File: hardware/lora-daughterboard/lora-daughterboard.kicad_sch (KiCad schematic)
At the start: 65 parts, among them J2 USB4110GFA, J6 Conn_01x04, J8 CON-SMA-EDGE-S, U14 E220-900MM22S, U22 W25Q64JVXGIQ TR, U28 ESP32-S3, U3 TPS62913RPUR, Y5 ECS-.327-6-16R-TR, Y6 ECS-400-10-37B2-CKY-TR

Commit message: hardware: BOM-cost pass across all four boards
Component changes from a cross-board cost review. Per-board component cost
(USD @~100qty): rocket $86.21 -> $61.39, base station $35.91 -> $29.89, with
the LoRa daughterboard and GNSS SAM-M10Q board added to the shared BOM.

Memory architecture
  - Rocket: MR25H10 MRAM deleted; the log ring moves to in-package PSRAM.
    ESP32-S3 -> ESP32-S3RH2 (2 MB quad PSRAM, no in-package flash, same land
    pattern; SPICS1/GPIO26 was already unconnected on every board).
    Persistence across boots is knowingly given up.
  - Rocket NAND F35SQB004G-WWT -> GD5F2GQ5UEYIGR: pin- and footprint-identical
    (verified against the U11 land pattern), 4 Gbit -> 2 Gbit, $11.61 -> $3.50.
    Needs the 4096 -> 2048 B page migration in firmware.
  - Base station: dedicated log flash deleted entirely. It wrote one ~183 B CSV
    row per received packet at the 2 Hz downlink (~366 B/s, and only while a
    flight is active), so 256 MB was ~204 hours of headroom. The firmware
    already falls back to the existing SPIFFS partition, so this promotes a
    tested path rather than needing new code.
  - Boot flash W25Q64JVXGIQ -> W25Q128JVSIQ on all four positions: 16 MB for
    LESS money ($3.10 -> $2.21). SCHEMATIC ONLY - the boards still need
    "Update PCB from Schematic" plus re-placement, since SOIC-8 208mil is 2.2x
    the DFN's area. The DFN's 9th (exposed) pad was a redundant GND tie; pin 4
    is GND on all four, so nothing is lost.

Power
  - LoRa + GNSS keep TPS62913 (low-noise, RF rails). The rocket briefly moved
    to it and was REVERTED to TPS62152: the TPS62913 is forced-PWM with 5 mA
    quiescent, which would have raised the pad-idle floor ~6x against the
    light-sleep work.
  - Base load switch TPS22810 -> TPS22918 (identical footprint and pin order;
    pin 3 EN/UVLO -> ON is safe because it was driven as a plain enable).
    CT cap 10 nF -> 2.2 nF to match the rocket's ramp; R8 (QOD->VOUT) deleted.
  - LoRa gains a 7.5k S-CONF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
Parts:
- removed CR1, CR3: PMEG2010ER_115, Footprints:DIODE_PMEG2010ER_115_NEX, symbol Custom:PMEG2010ER_115
- removed L1: ASPI-0530HI-2R2M-T2, Footprints:IND_ASPI-0530HI-2R2M-T2, symbol Custom:ASPI-0530HI-2R2M-T2
- added CR1, CR3: CUS10S30_H3F, USC_TOS, symbol Custom:CUS10S30_H3F
- added L8: VLS3012CX-2R2M-1, Footprints:IND_VLS3012CX-2R2M-1, symbol Custom:VLS3012CX-2R2M-1
- added R8: 7.5 k, Resistor_SMD:R_0402_1005Metric, symbol Device:R_US
- C102: value 47 uF -> 10 uF
- C106: value 22 uF -> 10 uF
- C16: value 10 uF -> 22 uF
- U22: value W25Q64JVXGIQ TR -> W25Q128JVSIQ; footprint Footprints:DFN_XGIQ TR_WIN -> Footprints:SOIC-8_W25Q128JVSIQ
- U28: value ESP32-S3 -> ESP32-S3RH2
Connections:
- net +BATT: now also CR3.2
- net GND: now also R8.2; no longer U3.10 (S-CONF)
- net VBUS: now also CR1.2
- net VSYS: now also CR1.1, CR3.1
- net at C11.1, C13.1, FB1.1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: now also L8.2
- net at U3.2 (SW): now also L8.1
- new net: R8.1, U3.10 (S-CONF)
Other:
- moved on the sheet: R4

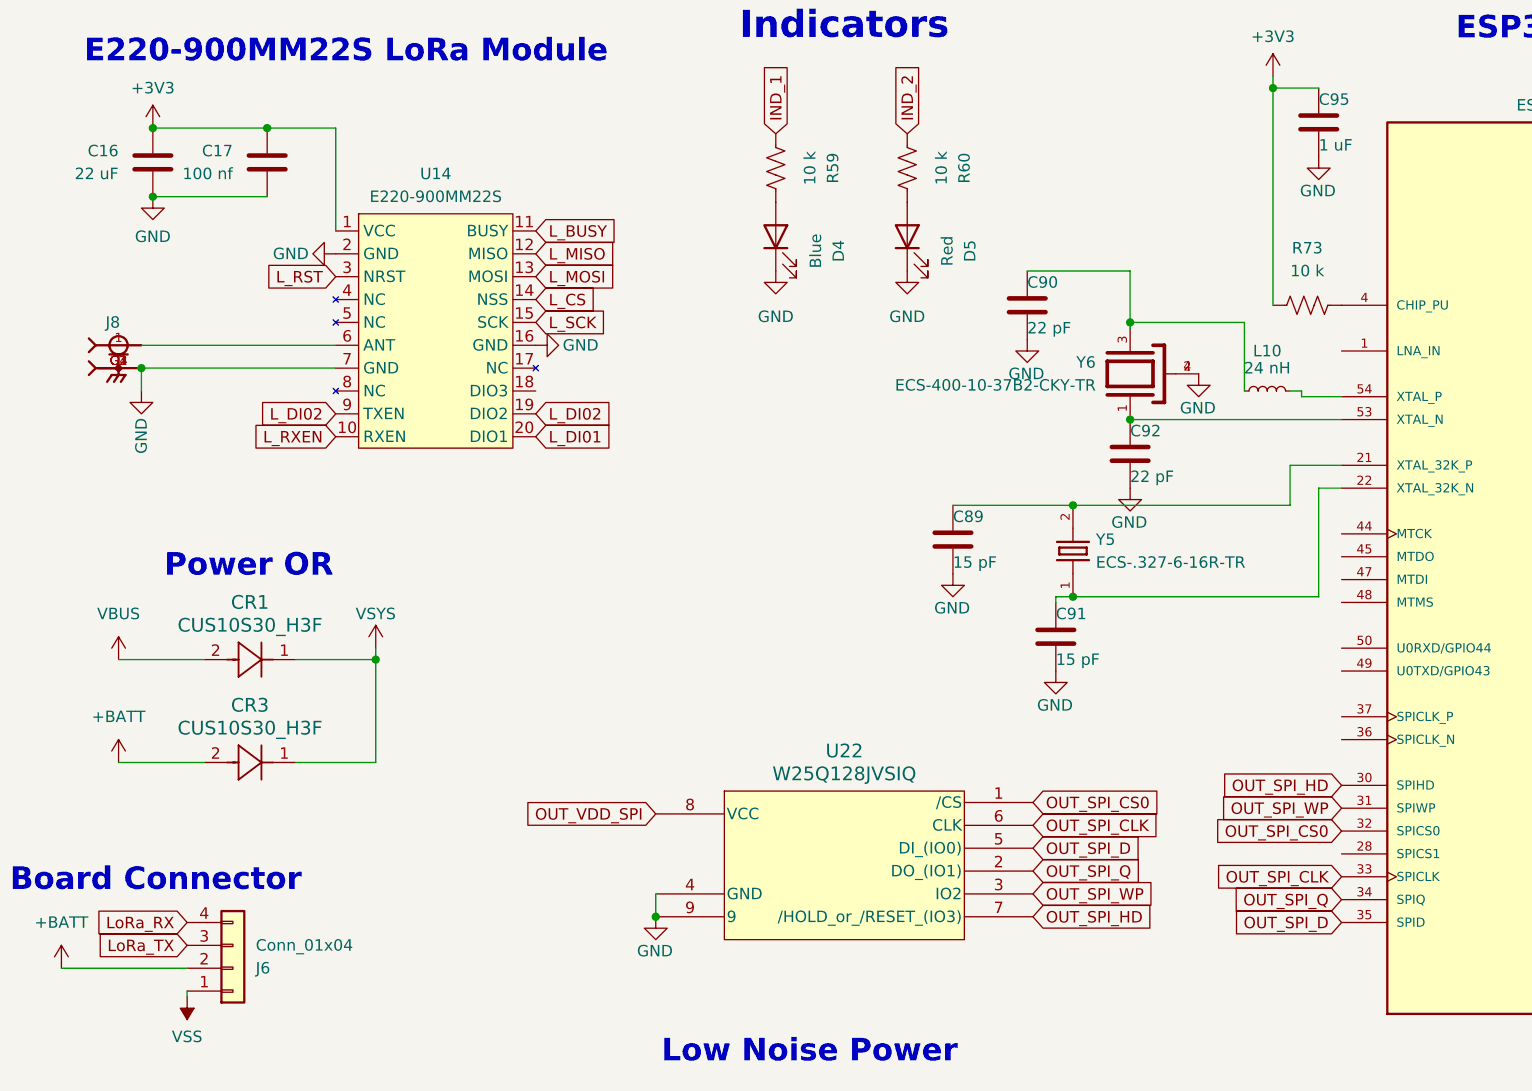
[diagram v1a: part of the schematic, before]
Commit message: hardware: battery protection, boost swap, and a capacitor voltage audit
Base station power chain, all verified against exported netlists:

- Protection: MAX17303G+ gauge/protector and its NTMD6N02R2G FET pair
  replaced by DW01A + 2x FS8205A. The MAX17303 had no firmware driver and
  the board never had a working coulomb counter, so state of charge already
  came from the voltage curve in bs_battery_soc.h; it now reads a 1M/1M
  divider on GPIO1. The FETs move from the positive rail to the negative
  one because the DW01A has no charge pump, so board ground is now P-,
  separated from the cell's B- by the FET stack. Two FS8205A in parallel
  put the 150 mV overcurrent trip at ~4.8-6.0 A instead of ~2.4-3.0 A.
  TH1 moves onto the BQ21040's TS pin, replacing a fixed 10k that had been
  defeating thermal charge cutoff.

- V_LORA retargeted 7.49 V -> 4.95 V and LM5157QRTERQ1 -> TPS61023DRLR.
  Nothing needed 7.4 V (everything downstream is 3.3 V behind the
  TPS62913), while an RFD868x-class radio is 5 V nominal with a 6 V
  absolute maximum, so the old rail put it permanently out of reach. Being
  synchronous and internally compensated also dropped D2, C35-C38 and R10.
  Inductor stays the fleet 2.2 uH: inside TI's 0.37-2.9 uH range and the
  only value meeting their ripple-under-40%-of-average guidance at load.

- Keystone 1043P holder -> MYOUNG BH-18650-A5BJ001-2D. Terminal pitch
  72.30 vs 72.22 mm, so the battery nets did not move; BT2 is rotated 180
  degrees because this part's positive end is mirrored.

Across all four boards:

- Every crystal was mis-loaded. 32.768 kHz parts saw ~9 pF against a 6 pF
  spec and the 40 MHz saw 12.5 pF against 10 pF, both pulling slow. Moved
  to Seiko SC-32S (12.5 pF) with 22 pF load caps, and the 40 MHz caps to
  18 pF. The tolerance being paid for had been swamped several times over.

- Capacitor voltage audit, new Min V rating column in the BOM. Three parts
  were operating outside their rating on 8.4 V rails: 47 uF and 100 u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
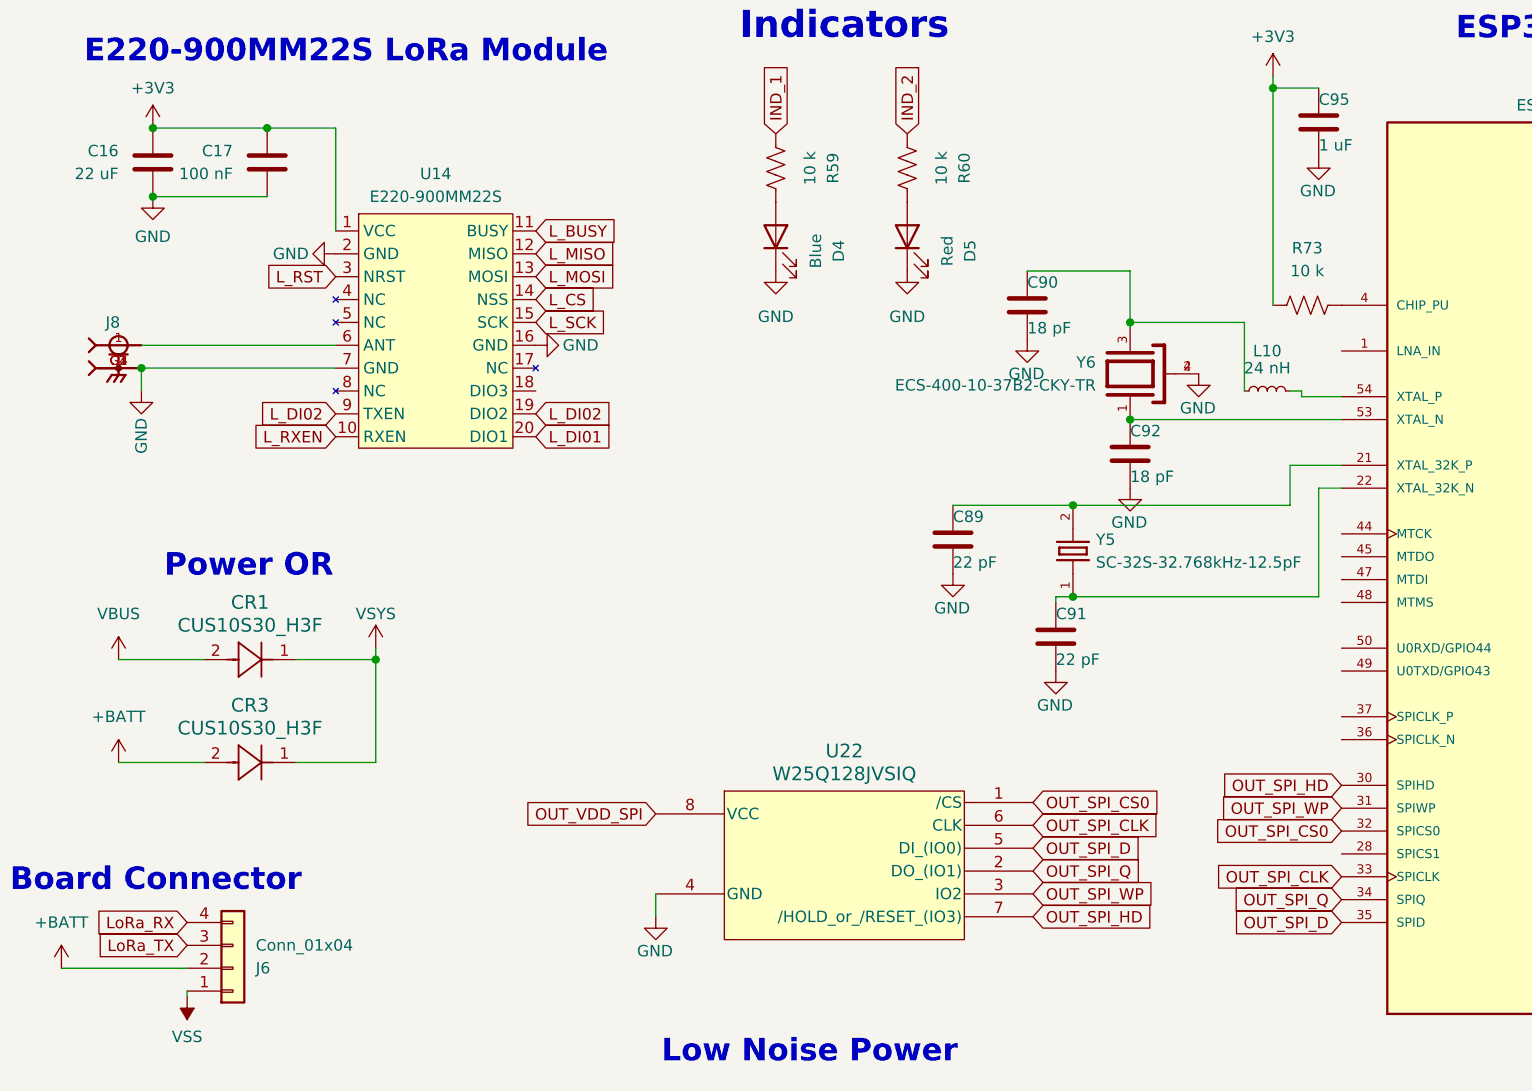
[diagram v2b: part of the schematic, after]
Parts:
- C17: value 100 nf -> 100 nF
- C89, C91: value 15 pF -> 22 pF
- C90, C92: value 22 pF -> 18 pF
- CR1, CR3: footprint USC_TOS -> Footprints:USC_TOS
- U22: symbol Custom:W25Q64JVXGIQ_TR -> Custom:W25Q128JVSIQ
- Y5: value ECS-.327-6-16R-TR -> SC-32S-32.768kHz-12.5pF; footprint Footprints:XTAL_ECS-.327-6-16R-TR -> Footprints:XTAL_SC-32S_3215; symbol Custom:ECS-.327-6-16R-TR -> Custom:SC-32S-32.768kHz-12.5pF
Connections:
- net GND: no longer U22.9
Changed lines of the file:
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@@
 	)
 	(junction
-		(at 86.36 118.745)
-		(diameter 0)
-		(color 0 0 0 0)
-	)
-	(junction
 		(at 70.485 160.655)
 		(diameter 0)
@@
 			)
 		)
-		(property "Value" "22 pF"
+		(property "Value" "18 pF"
 			(at 127.635 53.34 0)
 			(show_name no)
@@
 			)
 		)
-		(property "Footprint" "USC_TOS"
+		(property "Footprint" "Footprints:USC_TOS"
 			(at 36.195 90.17 0)
 			(hide yes)
@@
 			)
 		)
-		(property "Footprint" "USC_TOS"
+		(property "Footprint" "Footprints:USC_TOS"
 			(at 36.195 101.6 0)
 			(hide yes)
@@
 			)
 		)
-		(property "Value" "15 pF"
+		(property "Value" "22 pF"
 			(at 130.81 90.17 0)
 			(show_name no)
@@
 	)
 	(symbol
-		(lib_id "Custom:W25Q64JVXGIQ_TR")
+		(lib_id "Custom:W25Q128JVSIQ")
 		(at 63.5 112.395 0)
 		(unit 1)
@@
 			)
 		)
-		(pin "9"
-		)
 		(pin "8"
 		)
@@
 			)
 		)
-		(property "Value" "22 pF"
+		(property "Value" "18 pF"
 			(at 139.065 69.85 0)
 			(show_name no)
@@
 			)
 		)
-		(property "Value" "15 pF"
+		(property "Value" "22 pF"
 			(at 119.38 79.375 0)
 			(show_name no)
@@
 	)
 	(symbol
-		(lib_id "Custom:ECS-.327-6-16R-TR")
+		(lib_id "Custom:SC-32S-32.768kHz-12.5pF")
 		(at 132.715 78.105 90)
 		(unit 1)
@@
 			)
 		)
-		(property "Value" "ECS-.327-6-16R-TR"
+		(property "Value" "SC-32S-32.768kHz-12.5pF"
 			(at 135.255 79.3749 90)
 			(show_name no)
@@
 			)
 		)
-		(property "Footprint" "Footprints:XTAL_ECS-.327-6-16R-TR"
+		(property "Footprint" "Footprints:XTAL_SC-32S_3215"
 			(at 132.715 78.105 0)
 			(hide yes)
@@
 			)
 		)
-		(property "Value" "100 nf"
+		(property "Value" "100 nF"
 			(at 39.37 36.1949 0)
 			(show_name no)

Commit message: hardware(lora): capacitor MPNs in KiCad + COUT 2x47uF -> 3x22uF
Capacitors: all 27 now carry MPN / Mfr / MinVRating fields, sourced from
Circuit Board BOMs/TinkerRocket_CrossBoard_BOM.xlsx (sheet "Cross-Board
BOM"). Field names mirror the spreadsheet columns so the two stay
diff-checkable; MinVRating is the design requirement, not the part's own
rating (the 470 nF requirement is 6.3 V while CL05A474KP5NNNC is a 10 V
part).

COUT: C11/C13 were CL21A476MQYNNNE (47 uF, 6.3 V X5R, 0805) on
Net-(U3-VO). At 3.3 V that is 52% of rated voltage, where the class
derates 55-70% -- roughly 28-42 uF against the TPS62913's 40 uF minimum
effective COUT. Revalued to CL21A226MOQNNNE (22 uF, 16 V), already a
stocked line on this board, and a third added (C14 + #PWR096 + junction
on the VO wire) for ~42-53 uF. Matches TI Table 8-5 (3 x 22 uF 0805).

Verified with kicad-cli under identical project context: nets unchanged
apart from the intended C14 addition (Net-(U3-VO) = C11.1 C13.1 C14.1
FB1.1 L8.2 R4.2 U3.3), ERC 301 -> 304 with the error count unchanged at
32 -- the three new warnings are endpoint_off_grid / lib_symbol_mismatch
inherited from the C13 and #PWR013 templates they were cloned from.

PCB not touched: needs Update PCB from Schematic, then place C14 (free
F.Cu slot at (93.40,128.8), inside the existing Net-(U3-VO) pour) and
re-route C95, whose schematic side moved to the CHIP_PU node.

Co-Authored-By: Claude Opus 5 <noreply@anthropic.com>
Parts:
- added C14: 22 uF, Capacitor_SMD:C_0805_2012Metric, symbol Device:C
- C10: MPN (none) -> CL05A474KP5NNNC; Mfr (none) -> Samsung; MinVRating (none) -> 6.3 V
- C100, C105, C95, C96: MPN (none) -> CL05A105KO5NNNC; Mfr (none) -> Samsung; MinVRating (none) -> 16 V
- C101, C103, C104, C17, C99: MPN (none) -> CL05B104KO5NNNC; Mfr (none) -> Samsung; MinVRating (none) -> 16 V
- C102, C106, C97: MPN (none) -> CL05A106MQ5NUNC; Mfr (none) -> Samsung; MinVRating (none) -> 6.3 V
- C11, C13: value 47 uF -> 22 uF; MPN (none) -> CL21A226MOQNNNE; Mfr (none) -> Samsung; MinVRating (none) -> 16 V
- C12, C15, C16, C8, C9: MPN (none) -> CL21A226MOQNNNE; Mfr (none) -> Samsung; MinVRating (none) -> 16 V
- C7: MPN (none) -> CC0402KRX7R9BB222; Mfr (none) -> Yageo; MinVRating (none) -> 16 V
- C89, C91: MPN (none) -> CL05C220JB5NNNC; Mfr (none) -> Samsung; MinVRating (none) -> 6.3 V
- C90, C92: MPN (none) -> CL05C180JB5NNNC; Mfr (none) -> Samsung; MinVRating (none) -> 6.3 V
- C98: MPN (none) -> CL05B103KB5NNNC; Mfr (none) -> Samsung; MinVRating (none) -> 6.3 V
- FB1: value WE-CBA_0805 -> 782853200
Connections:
- net +3V3: now also R73.1; no longer C95.1, R73.2
- net GND: now also C14.2
- net at U28.4 (CHIP_PU): now also C95.1, R73.2; no longer R73.1
- net at C11.1, C13.1, FB1.1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: now also C14.1
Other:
- moved on the sheet: C95, R73

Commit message: hardware(lora): VDD_SPI -- flash to +3V3, decoupling to the pin
Pre-fab review finding 4. In 3.3 V mode VDD_SPI is not a regulator: the
S3 datasheet Table 5-3 describes it as "VDD_SPI powered by VDD3P3_RTC via
R_SPI", 14 ohm typ, and footnote 2 bounds the load with

    VDD3P3_RTC > VDD_flash_min + I_flash_max * R_SPI

On the S3RH2 the in-package 2 MB quad PSRAM already sits on that node
(Table 1-1), so I_flash_max is flash plus PSRAM. Flash alone passes
comfortably (2.7 + 0.025*14 = 3.05 V required, 3.3 V available); flash
plus PSRAM at ~30 mA does not (3.47 V required). Espressif publishes no
in-package PSRAM current figure, so that second number is an estimate --
this change is defensive, removing a coupling where enabling
CONFIG_SPIRAM later would silently starve the boot flash.

  - U22 pin 8 (VCC): OUT_VDD_SPI -> +3V3
  - C18 100 nF added on +3V3 as the flash's local decoupling
  - OUT_VDD_SPI left as {U28.29, C96 1 uF, C97 10 uF}, serving only PSRAM

C97 stays at 10 uF deliberately. The HDG's "do not add excessively large
capacitors" is driven by startup delay through the 14 ohm and by
light-sleep wake recovery; neither applies here (VDD_SPI settles in
~400 us against a 2-3 ms CHIP_PU release, and this board never
light-sleeps). Meanwhile the 14 ohm makes VDD_SPI the highest-source-
impedance rail on the board, where local bulk is worth most.

Verified: OUT_VDD_SPI = {C96.1, C97.1, U28.29}; ERC error count unchanged
at 32 (one power_pin_not_driven moved from U22.8 to U28.29, the existing
missing-PWR_FLAG class).

PCB pending: move C96/C97 to U28 pin 29 at (86.20,115.76) and place C18
where they were, next to U22 pin 8 at (90.61,114.05).

Co-Authored-By: Claude Opus 5 <noreply@anthropic.com>
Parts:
- added C18: 100 nF, Capacitor_SMD:C_0402_1005Metric, symbol Device:C
- added R77, R78: 1 k, Resistor_SMD:R_0402_1005Metric, symbol Device:R_US
- C90, C92: value 18 pF -> 12 pF; MPN CL05C180JB5NNNC -> CL05C120JB5NNNC
- C96: value 1 uF -> 10 uF
- C97: value 10 uF -> 100 nF; MPN CL05A106MQ5NUNC -> CL05B104KO5NNNC; MinVRating 6.3 V -> 16 V
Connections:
- net +3V3: now also U22.8 (VCC), C18.1
- net GND: now also C18.2
- net LoRa_RX: now also R77.1; no longer J6.4 (Pin_4)
- net LoRa_TX: now also R78.1; no longer J6.3 (Pin_3)
- net OUT_VDD_SPI: no longer U22.8 (VCC)
- new net: J6.3 (Pin_3), R78.2
- new net: J6.4 (Pin_4), R77.2
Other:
- moved on the sheet: J6

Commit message: hardware: silkscreen outlines for Y6, J8 and U3; fiducials FID3/FID4
Pre-fab review findings 10 and 11, LoRa daughterboard.

Finding 11 is largely withdrawn -- every orientation- and polarity-critical
part already carried silkscreen, and printing RXX/CXX designators on a
22 x 27.5 mm board neither fits nor helps. Two genuine gaps remained:
Y6 (4-pad crystal, pins 1/3 are the terminals and 2/4 case ground, so
orientation matters) and J8 (the RF connector) had no silk at all. U3
picked one up in the same pass.

Finding 10 restated: the FID1-inside-J2 courtyard overlap is not the issue
-- fiducials are read on a bare board before placement, so being inside a
connector's courtyard does not obscure one when it is used. The real gap
was count: one per side gives translation correction only, with no rotation
or scale reference for a 0.4 mm-pitch QFN-56. FID3 and FID4 added.

Co-Authored-By: Claude Opus 5 <noreply@anthropic.com>
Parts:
- added FID3, FID4, FID5, FID6: Fiducial, Fiducial:Fiducial_0.5mm_Mask1mm, symbol Mechanical:Fiducial
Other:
- moved on the sheet: FID1, FID2
